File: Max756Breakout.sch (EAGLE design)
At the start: 8 parts

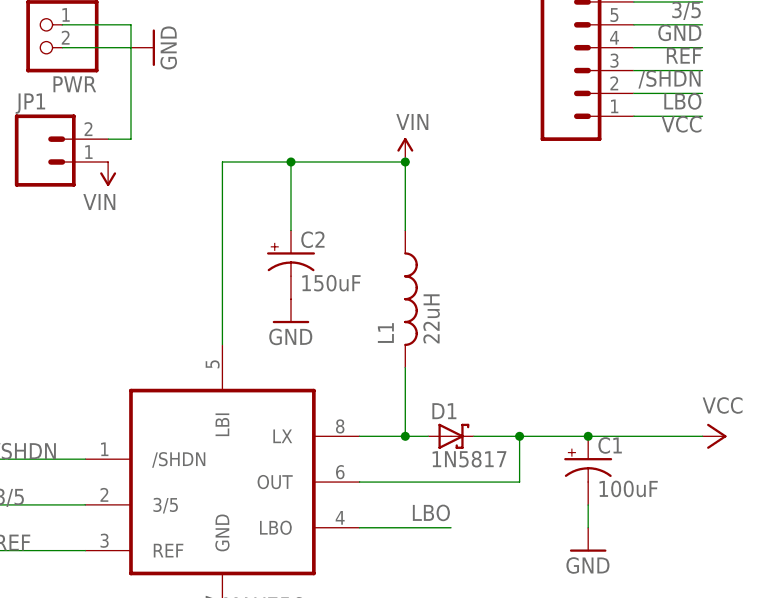
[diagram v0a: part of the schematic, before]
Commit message: Replaced some parts with better real world representations
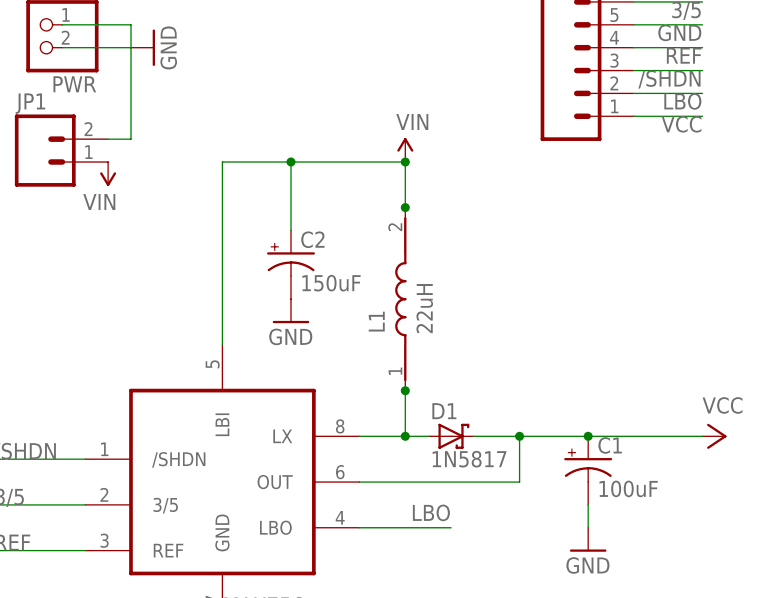
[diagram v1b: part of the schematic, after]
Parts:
- D1: device adafruit:SCHOTTKY-DIODECB417-15 -> Dek:SCHOTTKY-DIODEF126Z12
- L1: device resistor:L-US0207/2V -> Dek:82114R
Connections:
- net L1: now also L1.1; no longer L1.2
- net VIN: now also L1.2; no longer L1.1
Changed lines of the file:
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@@
 <setting verticaltext="up"/>
 </settings>
-<grid distance="0.1" unitdist="inch" unit="inch" style="lines" multiple="1" display="no" altdistance="0.01" altunitdist="inch" altunit="inch"/>
+<grid distance="0.05" unitdist="inch" unit="inch" style="lines" multiple="1" display="yes" altdistance="0.005" altunitdist="inch" altunit="inch"/>
 <layers>
 <layer number="1" name="Top" color="4" fill="1" visible="yes" active="no"/>
@@
 <layer number="23" name="tOrigins" color="15" fill="1" visible="yes" active="no"/>
 <layer number="24" name="bOrigins" color="15" fill="1" visible="yes" active="no"/>
-<layer number="25" name="tNames" color="7" fill="1" visible="yes" active="no"/>
+<layer number="25" name="tNames" color="16" fill="1" visible="yes" active="no"/>
 <layer number="26" name="bNames" color="7" fill="1" visible="yes" active="no"/>
 <layer number="27" name="tValues" color="7" fill="1" visible="yes" active="no"/>
@@
 <part name="C2" library="SparkFun-Capacitors" deviceset="CAP_POL" device="PTH1" value="150uF"/>
 <part name="GND1" library="supply1" deviceset="GND" device=""/>
-<part name="D1" library="adafruit" deviceset="SCHOTTKY-DIODE" device="CB417-15" value="1N5817"/>
 <part name="GND2" library="supply1" deviceset="GND" device=""/>
 <part name="GND3" library="supply1" deviceset="GND" device=""/>
@@
 <part name="JP2" library="SparkFun-Connectors" deviceset="M07" device="LOCK_LONGPADS"/>
 <part name="PWR" library="adafruit" deviceset="JST_2PIN" device="-THM-RA" value="PWR"/>
-<part name="L1" library="resistor" deviceset="L-US" device="0207/2V" value="22uH"/>
 <part name="JP1" library="SparkFun-Connectors" deviceset="M02" device="LOCK_LONGPADS"/>
 <part name="SUPPLY4" library="SparkFun-Aesthetics" deviceset="VIN" device=""/>
+<part name="L1" library="Dek" deviceset="82114R" device="" value="22uH"/>
+<part name="D1" library="Dek" deviceset="SCHOTTKY-DIODE" device="F126Z12" value="1N5817"/>
 </parts>
 <sheets>
@@
 <instance part="C2" gate="G$1" x="66.04" y="73.66"/>
 <instance part="GND1" gate="1" x="99.06" y="40.64"/>
-<instance part="D1" gate="G$1" x="83.82" y="53.34"/>
 <instance part="GND2" gate="1" x="66.04" y="66.04"/>
 <instance part="GND3" gate="1" x="58.42" y="30.48"/>
@@
 <instance part="JP2" gate="G$1" x="99.06" y="93.98"/>
 <instance part="PWR" gate="G$1" x="38.1" y="99.06" rot="R180"/>
-<instance part="L1" gate="G$1" x="78.74" y="68.58"/>
 <instance part="JP1" gate="G$1" x="38.1" y="83.82"/>
 <instance part="SUPPLY4" gate="G$1" x="45.72" y="83.82" rot="R180"/>
+<instance part="L1" gate="1" x="78.74" y="68.58" rot="R90"/>
+<instance part="D1" gate="G$1" x="83.82" y="53.34"/>
 </instances>
 <busses>
@@
 <segment>
 <pinref part="MAX756" gate="G$1" pin="LX"/>
-<pinref part="D1" gate="G$1" pin="A"/>
 <wire x1="81.28" y1="53.34" x2="78.74" y2="53.34" width="0.1524" layer="91"/>
 <wire x1="78.74" y1="53.34" x2="73.66" y2="53.34" width="0.1524" layer="91"/>
-<wire x1="78.74" y1="60.96" x2="78.74" y2="53.34" width="0.1524" layer="91"/>
+<wire x1="78.74" y1="58.42" x2="78.74" y2="58.406" width="0.1524" layer="91"/>
 <junction x="78.74" y="53.34"/>
-<pinref part="L1" gate="G$1" pin="2"/>
+<pinref part="L1" gate="1" pin="1"/>
+<wire x1="78.74" y1="58.406" x2="78.74" y2="53.34" width="0.1524" layer="91"/>
+<junction x="78.74" y="58.406"/>
+<pinref part="D1" gate="G$1" pin="A"/>
 </segment>
 </net>
@@
 <wire x1="58.42" y1="83.82" x2="66.04" y2="83.82" width="0.1524" layer="91"/>
 <wire x1="66.04" y1="83.82" x2="78.74" y2="83.82" width="0.1524" layer="91"/>
-<wire x1="78.74" y1="83.82" x2="78.74" y2="76.2" width="0.1524" layer="91"/>
 <pinref part="C2" gate="G$1" pin="+"/>
 <wire x1="66.04" y1="76.2" x2="66.04" y2="83.82" width="0.1524" layer="91"/>
 <junction x="66.04" y="83.82"/>
 <pinref part="SUPPLY1" gate="G$1" pin="VIN"/>
+<wire x1="78.74" y1="78.74" x2="78.74" y2="78.754" width="0.1524" layer="91"/>
 <junction x="78.74" y="83.82"/>
-<pinref part="L1" gate="G$1" pin="1"/>
+<pinref part="L1" gate="1" pin="2"/>
+<wire x1="78.74" y1="78.754" x2="78.74" y2="83.82" width="0.1524" layer="91"/>
+<junction x="78.74" y="78.754"/>
 </segment>
 <segment>
@@
 <segment>
 <pinref part="C1" gate="G$1" pin="+"/>
-<pinref part="D1" gate="G$1" pin="C"/>
 <wire x1="86.36" y1="53.34" x2="91.44" y2="53.34" width="0.1524" layer="91"/>
 <pinref part="MAX756" gate="G$1" pin="OUT"/>
@@
 <junction x="99.06" y="53.34"/>
 <pinref part="P+1" gate="VCC" pin="VCC"/>
-</segment>
-<segment>
+<pinref part="D1" gate="G$1" pin="C"/>
+</segment>
+<segment>

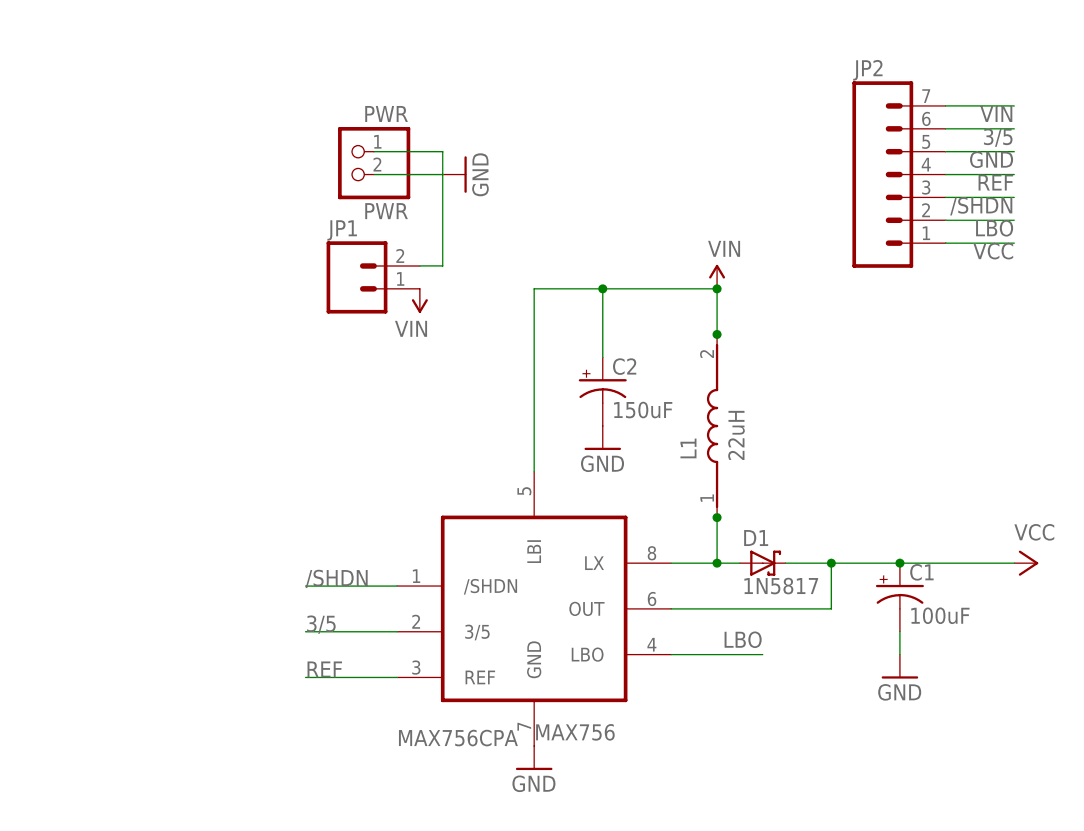
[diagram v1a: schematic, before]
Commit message: Changed voltage selector to a jumper
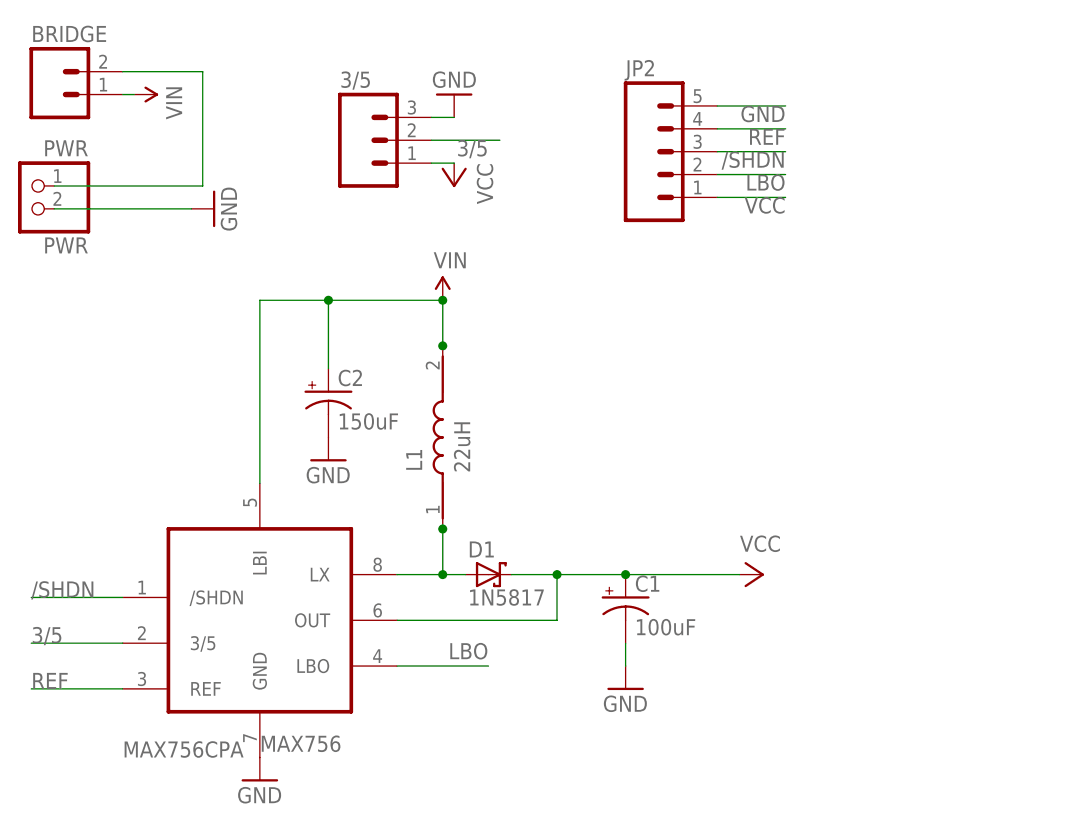
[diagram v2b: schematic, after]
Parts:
- removed JP1: (no value), SparkFun-Connectors:M02LOCK_LONGPADS
- added 3/5: (no value), SparkFun-Connectors:M03LOCK
- added BRIDGE: (no value), SparkFun-Connectors:M02LOCK
- JP2: device SparkFun-Connectors:M07LOCK_LONGPADS -> SparkFun-Connectors:M05LOCK
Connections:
- net 3/5: now also 3/5.2; no longer JP2.6
- net GND: now also 3/5.3
- net N$1: now also BRIDGE.2; no longer JP1.2
- net VCC: now also 3/5.1
- net VIN: now also BRIDGE.1; no longer JP1.1, JP2.7
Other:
- moved on the sheet: C1, C2, D1, L1, MAX756, PWR

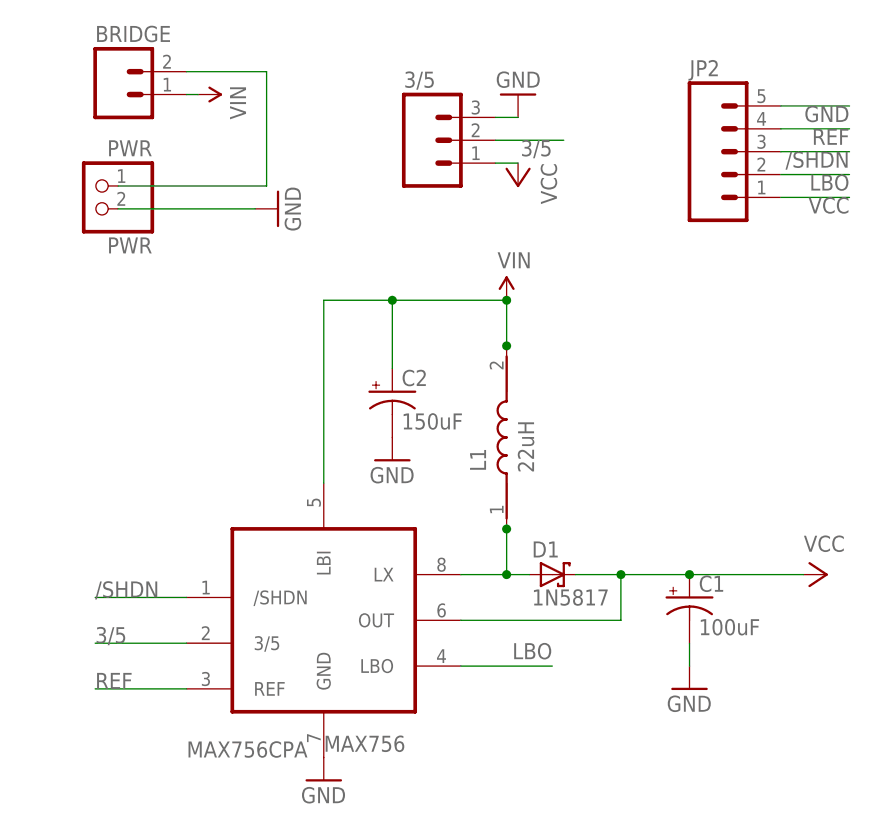
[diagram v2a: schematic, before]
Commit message: Only breakout 2 pins for ease of use
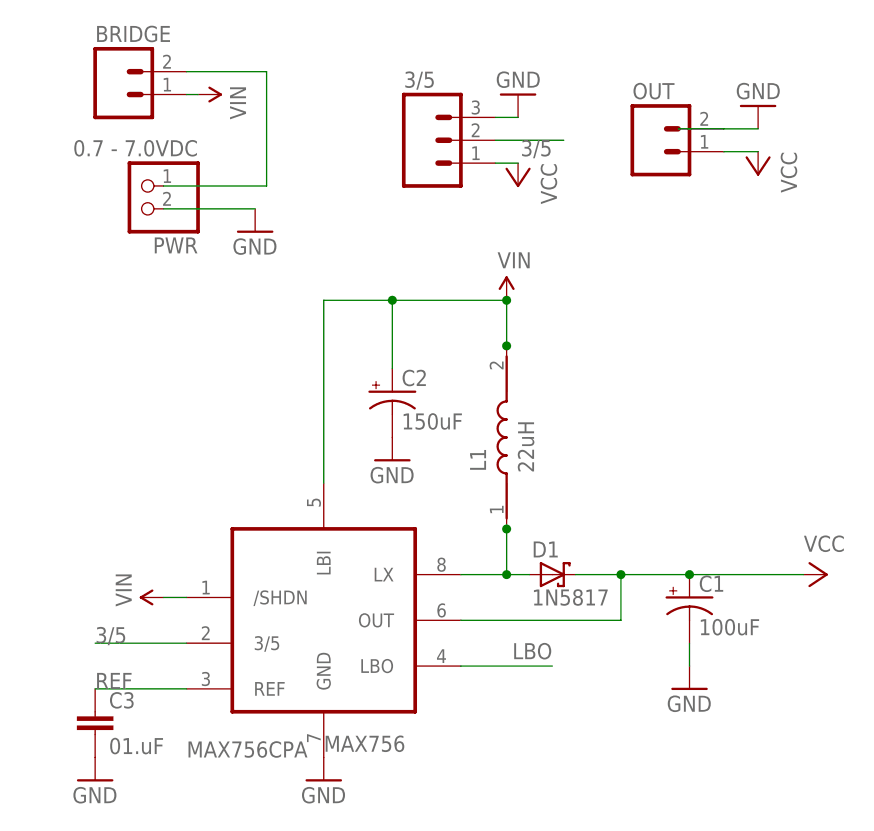
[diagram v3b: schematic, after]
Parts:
- removed JP2: (no value), SparkFun-Connectors:M05LOCK
- added C3: 01.uF, Dek:CAPPTH2
- added OUT: (no value), SparkFun-Connectors:M02LOCK
- PWR: value PWR -> 0.7 - 7.0VDC; device adafruit:JST_2PIN-THM-RA -> Dek:JST_2PIN-THM-RA
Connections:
- removed net /SHDN: JP2.3, MAX756./SHDN
- net GND: now also C3.2, OUT.2; no longer JP2.5
- net LBO: no longer JP2.2
- net REF: now also C3.1; no longer JP2.4
- net VCC: now also OUT.1; no longer JP2.1
- net VIN: now also MAX756./SHDN
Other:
- moved on the sheet: PWR
